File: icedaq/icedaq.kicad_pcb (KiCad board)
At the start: 2 copper layers, 53 parts, among them J1 analog outputs, J2 analog inputs, P1 UART, U1 REG12, U2 iCE40HX1K-VQ100, U3 RPi, U4 oscillator4, U5 ADC082S021, U6 ADC082S021, U7 MCP6004

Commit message: icedaq layout
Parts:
- added CD1: C_Small, Capacitors_SMD:C_0603_HandSoldering, F.Cu at (171.6, 81.3)
- added CD11: C_Small, Capacitors_SMD:C_0603_HandSoldering, F.Cu at (178.7, 97.6)
- added CD12: C_Small, Capacitors_SMD:C_0603_HandSoldering, F.Cu at (159.4, 87.1)
- added CD13: C_Small, Capacitors_SMD:C_0603_HandSoldering, F.Cu at (149.8, 63.2)
- added CD3: C_Small, Capacitors_SMD:C_0603_HandSoldering, F.Cu at (189.9, 65.7)
- added CD4: C_Small, Capacitors_SMD:C_0603_HandSoldering, F.Cu at (197.7, 79.6)
- added CD5: C_Small, Capacitors_SMD:C_0603_HandSoldering, F.Cu at (174.8, 80.9)
- added CD6: C_Small, Capacitors_SMD:C_0603_HandSoldering, F.Cu at (169.0, 68.8)
- added CD7: C_Small, Capacitors_SMD:C_0603_HandSoldering, F.Cu at (192.0, 88.3)
- added RB1: 3.9k, Resistors_SMD:R_0603_HandSoldering, F.Cu at (192.0, 65.6)
- added RB2: 3.9k, Resistors_SMD:R_0603_HandSoldering, F.Cu at (193.9, 66.3)
- added REF**: MountingHole_3mm, Mounting_Holes:MountingHole_3mm, F.Cu at (140.1, 58.7)
- added REF**: MountingHole_3mm, Mounting_Holes:MountingHole_3mm, F.Cu at (198.1, 58.7)
- added REF**: MountingHole_3mm, Mounting_Holes:MountingHole_3mm, F.Cu at (198.1, 107.7)
- added REF**: MountingHole_3mm, Mounting_Holes:MountingHole_3mm, F.Cu at (140.1, 107.7)
- added ROM1: CAT24C, Housings_SOIC:SOIC-8_3.9x4.9mm_Pitch1.27mm, F.Cu at (197.9, 65.6)
- moved R20 50.3 mm to (163.6, 108.5), turned to 0 degrees
- moved R22 46.6 mm to (157.4, 108.7), turned to 0 degrees
- moved D5 42.6 mm to (148.4, 102.2), turned to 270 degrees
- moved D6 42.3 mm to (150.7, 106.0)
- moved J2 42.2 mm to (140.8, 63.9)
- moved J1 40.5 mm to (140.6, 95.6)
- moved D3 39.7 mm to (151.8, 72.2), turned to 0 degrees
- moved D4 38.7 mm to (153.9, 75.2), turned to 0 degrees
- moved R1 38.5 mm to (186.4, 96.3)
- moved U4 37.4 mm to (186.5, 92.1), turned to 180 degrees
- moved R4 36.8 mm to (158.2, 103.1), turned to 180 degrees
- moved R3 36.7 mm to (158.1, 100.7), turned to 0 degrees
- moved R18 36.5 mm to (163.0, 103.1), turned to 0 degrees
- moved R17 36.4 mm to (163.1, 100.7), turned to 180 degrees
- moved R12 36.1 mm to (153.9, 78.0), turned to 180 degrees
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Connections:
- R1 pad 1: +3V3 -> Net-(R1-Pad1)
- R1 pad 2: Net-(R1-Pad2) -> +3V3
- U2 pad 30: /GCLK2 -> (no net)
- U2 pad 37: /MISO1 -> /SCLK1
- U2 pad 41: /SCLK1 -> /MISO1
- U2 pad 63: /Analog/clk -> GCLK2
- U2 pad 65: /Analog/din3 -> (no net)
- U2 pad 66: /Analog/slkc3 -> (no net)
- U2 pad 68: /Analog/sync3 -> (no net)
- U2 pad 71: /Analog/din4 -> (no net)
- U2 pad 72: /Analog/sclk4 -> (no net)
- U2 pad 73: /Analog/sync4 -> (no net)
- U2 pad 78: (no net) -> /Analog/din3
- U2 pad 79: (no net) -> /Analog/slkc3
- U2 pad 80: (no net) -> /Analog/sync3
- U2 pad 82: (no net) -> /Analog/din4
- U2 pad 83: (no net) -> /Analog/sclk4
- U2 pad 85: (no net) -> /Analog/sync4
- U2 pad 90: (no net) -> clk
- U3 pad 27: (no net) -> /ID_SD
- U3 pad 28: (no net) -> /ID_SC
- U3 pad 31: /GCLK2 -> /GCLK0
- U3 pad 7: /GCLK0 -> GCLK2
- U4 pad 1: Net-(R1-Pad2) -> Net-(R1-Pad1)
- U4 pad 3: /Analog/clk -> clk
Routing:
- net +3V3: track 0.00 -> 215.8 mm, vias 0 -> 5
- net GND: track 0.00 -> 107.5 mm, vias 0 -> 33
- net +5V: track 0.00 -> 85.7 mm, vias 0 -> 4
- net +1V2: track 0.00 -> 62.7 mm
- net /SS1: track 0.00 -> 38.3 mm, vias 0 -> 1
- net /CDONE: track 0.00 -> 36.2 mm, vias 0 -> 1
- net /Analog/in4a: track 0.00 -> 33.8 mm, vias 0 -> 3
- net /Analog/in2a: track 0.00 -> 33.7 mm, vias 0 -> 1
- net GCLK2: track 0.00 -> 33.6 mm, vias 0 -> 1
- net /CRST: track 0.00 -> 31.4 mm, vias 0 -> 1
- net /ID_SC: track 0.00 -> 31.3 mm
- net /ID_SD: track 0.00 -> 28.5 mm, vias 0 -> 2
- net /Analog/out4: track 0.00 -> 25.3 mm
- net /Analog/in1: track 0.00 -> 24.9 mm, vias 0 -> 1
- net /MOSI: track 0.00 -> 20.8 mm, vias 0 -> 1
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- added copper zone on B.Cu, net GND
- added copper zone on F.Cu, net GND
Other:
- board outline added: 65.3 x 56.4 mm
- net class Default: clearance 0.2 -> 0.1524; trace_width 0.25 -> 0.1778; via_dia 0.6 -> 0.5588; via_drill 0.4 -> 0.381
- net class Ground added: clearance 0.1524, trace_width 0.1778, via_dia 0.5588, via_drill 0.381
- net class Power added: clearance 0.2032, trace_width 0.3556, via_dia 0.762, via_drill 0.4826
- rule trace_clearance: 0.2 -> 0.1524
- rule trace_min: 0.2 -> 0.1524
- rule via_min_drill: 0.3 -> 0.3302
- rule via_min_size: 0.4 -> 0.508

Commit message: icedaq more
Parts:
- added P2: GPIO, Pin_Headers:Pin_Header_Straight_1x05_Pitch2.00mm, F.Cu at (199.0, 80.0)
- moved CD4 4.53 mm to (197.5, 84.1)
- moved U6 0.15 mm to (170.4, 72.1)
- moved U5 0.07 mm to (170.3, 77.0)
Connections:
- U2 pad 20: (no net) -> Net-(P2-Pad1)
- U2 pad 21: (no net) -> Net-(P2-Pad2)
- U2 pad 24: (no net) -> Net-(P2-Pad3)
- U2 pad 25: (no net) -> Net-(P2-Pad4)
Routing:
- net GND: track 107.5 -> 130.4 mm, vias 33 -> 41
- net Net-(P2-Pad1): track 0.00 -> 8.84 mm
- net Net-(P2-Pad3): track 0.00 -> 7.55 mm
- net Net-(P2-Pad2): track 0.00 -> 7.34 mm
- net Net-(P2-Pad4): track 0.00 -> 5.94 mm
- net +1V2: track 62.7 -> 60.6 mm
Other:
- outline, holes or cut-outs redrawn

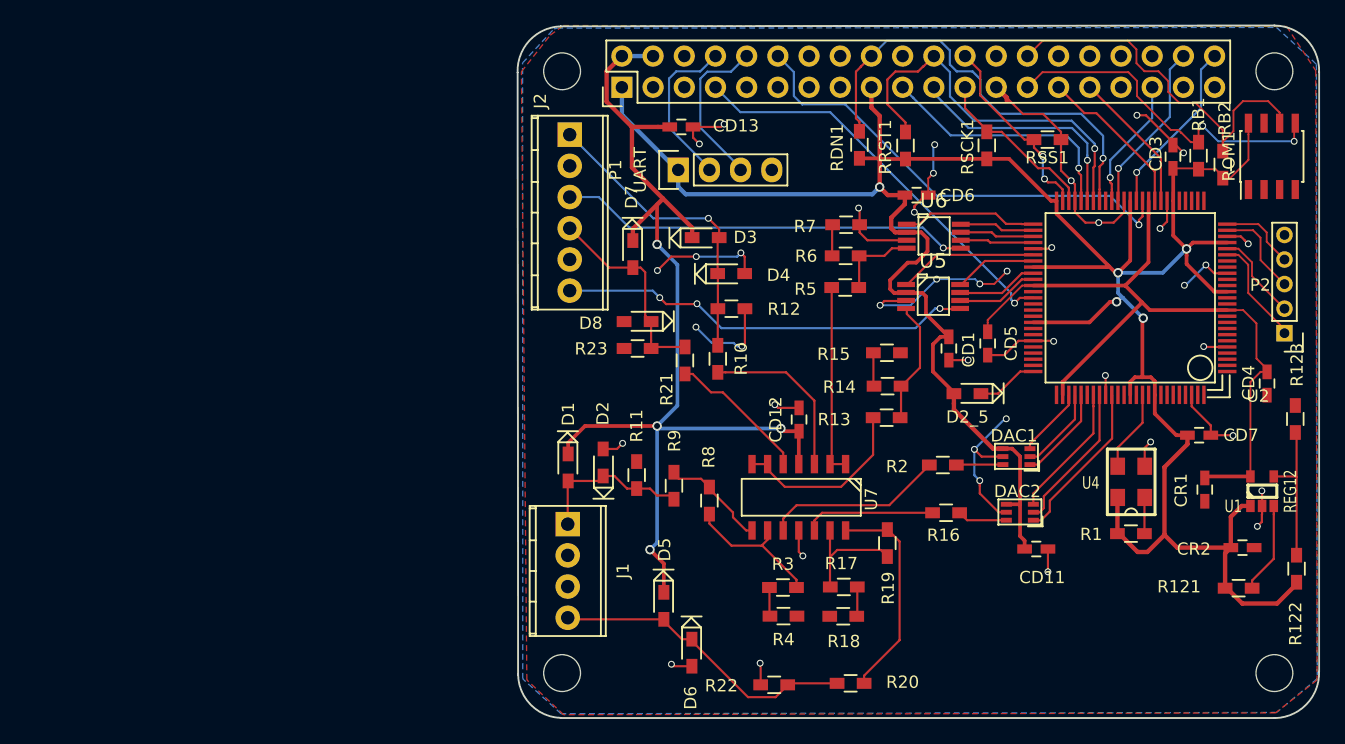
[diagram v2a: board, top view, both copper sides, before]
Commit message: icedaq: change input filter
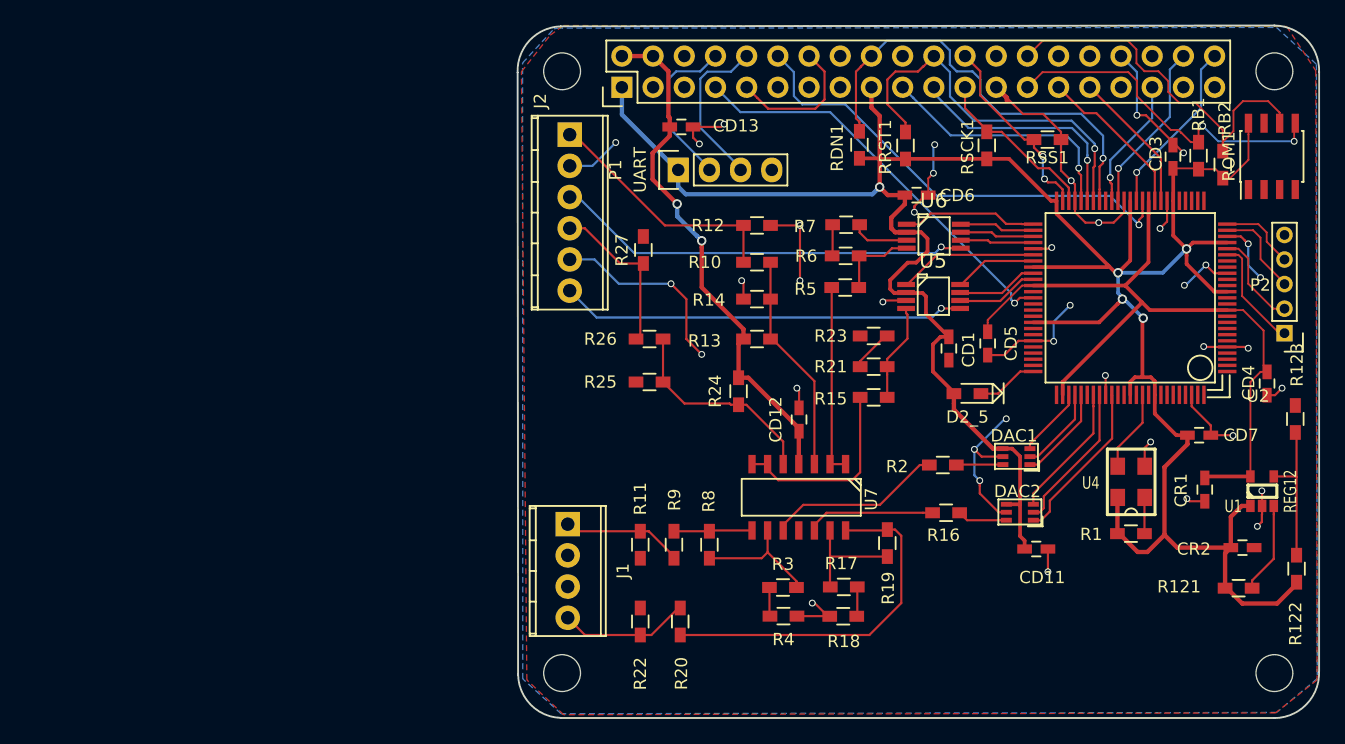
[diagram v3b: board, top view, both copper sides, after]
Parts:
- removed D1, D2, D3, D4, D5, D6, D7, D8: D_Small, local:D_0603_HandSoldering
- added R24: R, Resistors_SMD:R_0603_HandSoldering, F.Cu at (154.5, 84.8)
- added R25: R, Resistors_SMD:R_0603_HandSoldering, F.Cu at (147.2, 84.0)
- added R26: R, Resistors_SMD:R_0603_HandSoldering, F.Cu at (147.2, 80.5)
- added R27: R, Resistors_SMD:R_0603_HandSoldering, F.Cu at (146.8, 73.2)
- R13, R14: value 1k -> R
- R21, R23: value R -> 1k
- moved R23 19.2 mm to (165.5, 80.2)
- moved R21 15.4 mm to (165.5, 82.8), turned to 0 degrees
- moved R20 14.8 mm to (149.8, 103.5), turned to 270 degrees
- moved R14 12.8 mm to (156.0, 77.2)
- moved R13 12.3 mm to (156.0, 80.5)
- moved R22 12.1 mm to (146.5, 103.5), turned to 270 degrees
- moved R10 8.49 mm to (156.0, 74.2), turned to 0 degrees
- moved R12 7.09 mm to (156.0, 71.2)
- moved R11 5.68 mm to (146.5, 97.2), turned to 90 degrees
- moved R9 4.80 mm to (149.2, 97.2)
- moved R15 3.79 mm to (165.5, 85.2)
- moved R8 3.60 mm to (152.1, 97.2)
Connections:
- R13 pad 1: /Analog/in3a -> Net-(R10-Pad2)
- R13 pad 2: Net-(R13-Pad2) -> +5V
- R14 pad 1: Net-(R14-Pad1) -> GND
- R14 pad 2: /Analog/in3a -> Net-(R10-Pad2)
- R15 pad 1: GND -> /Analog/in3a
- R15 pad 2: Net-(R14-Pad1) -> Net-(R15-Pad2)
- R21 pad 1: /Analog/in3 -> Net-(R21-Pad1)
- R21 pad 2: Net-(R21-Pad2) -> /Analog/in3a
- R23 pad 2: /Analog/in3 -> Net-(R21-Pad1)
- U7 pad 5: Net-(R21-Pad2) -> Net-(R24-Pad1)
- U7 pad 6: Net-(R13-Pad2) -> Net-(R15-Pad2)
- U7 pad 7: Net-(R13-Pad2) -> Net-(R15-Pad2)
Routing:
- net +5V: track 85.7 -> 42.6 mm, vias 4 -> 2
- net GND: track 130.4 -> 152.1 mm, vias 41 -> 39
- net Net-(R24-Pad1): track 0.00 -> 17.1 mm
- net Net-(R15-Pad2): track 0.00 -> 16.0 mm
- net Net-(R13-Pad2): track 15.0 -> 0.00 mm
- net /Analog/out4: track 25.3 -> 10.7 mm
- net Net-(R19-Pad2): track 17.6 -> 29.3 mm
- net Net-(R21-Pad2): track 11.6 -> 0.00 mm
- net /Analog/in1: track 24.9 -> 20.2 mm, vias 1 -> 0
- net Net-(R10-Pad2): track 14.0 -> 18.0 mm
- net Net-(R21-Pad1): track 0.00 -> 3.50 mm
- net /Analog/in3: track 16.8 -> 13.6 mm
- net /Analog/out3: track 13.1 -> 9.89 mm
- net Net-(R14-Pad1): track 2.74 -> 0.00 mm
- net Net-(R8-Pad2): track 8.72 -> 6.38 mm
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
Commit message: icedaq: update
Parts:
- added TP1: WP, local:testpoint, F.Cu at (175.4, 62.4)
- J2: footprint Terminal_Blocks:TerminalBlock_Pheonix_MPT-2.54mm_6pol -> Terminal_Blocks:TerminalBlock_Pheonix_MPT-2.54mm_4pol
- moved CD7 23.3 mm to (199.2, 66.2), turned to 90 degrees
- moved RB2 23.2 mm to (170.8, 67.4)
- moved ROM1 22.0 mm to (176.0, 67.0)
- moved RSCK1 21.7 mm to (196.4, 65.6)
- moved CD5 17.7 mm to (187.6, 68.6), turned to 90 degrees
- moved RB1 11.4 mm to (180.6, 66.4)
- moved CD3 10.8 mm to (198.8, 71.8), turned to 0 degrees
- moved CD4 9.19 mm to (192.8, 92.0), turned to 180 degrees
- moved CR2 6.72 mm to (192.0, 103.2)
- moved R123 6.70 mm to (199.4, 93.7)
- moved R121 6.30 mm to (192.0, 106.2)
- moved U1 6.17 mm to (193.9, 99.8)
- moved P2 5.78 mm to (199.2, 85.8)
- moved CD11 5.29 mm to (177.8, 102.8)
- moved RSS1 4.80 mm to (184.2, 65.8), turned to 90 degrees
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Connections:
- J2 pad 3: /Analog/in2a -> GND
- ROM1 pad 7: (no net) -> Net-(ROM1-Pad7)
- U2 pad 1: (no net) -> Net-(U2-Pad1)
- U2 pad 10: (no net) -> Net-(P2-Pad4)
- U2 pad 100: (no net) -> Net-(U2-Pad100)
- U2 pad 12: (no net) -> Net-(U2-Pad12)
- U2 pad 13: (no net) -> Net-(U2-Pad13)
- U2 pad 15: (no net) -> Net-(U2-Pad15)
- U2 pad 16: (no net) -> Net-(U2-Pad16)
- U2 pad 18: (no net) -> Net-(U2-Pad18)
- U2 pad 19: (no net) -> Net-(U2-Pad19)
- U2 pad 2: (no net) -> Net-(U2-Pad2)
- U2 pad 20: Net-(P2-Pad1) -> Net-(U2-Pad20)
- U2 pad 21: Net-(P2-Pad2) -> Net-(U2-Pad21)
- U2 pad 24: Net-(P2-Pad3) -> Net-(U2-Pad24)
- U2 pad 25: Net-(P2-Pad4) -> Net-(U2-Pad25)
- U2 pad 26: (no net) -> Net-(U2-Pad26)
- U2 pad 27: (no net) -> Net-(U2-Pad27)
- U2 pad 28: (no net) -> Net-(U2-Pad28)
- U2 pad 29: (no net) -> Net-(U2-Pad29)
- U2 pad 3: (no net) -> Net-(U2-Pad3)
- U2 pad 30: (no net) -> Net-(U2-Pad30)
- U2 pad 36: /SS1 -> Net-(U2-Pad36)
- U2 pad 37: /SCLK1 -> Net-(U2-Pad37)
- U2 pad 4: (no net) -> Net-(U2-Pad4)
- U2 pad 40: /MOSI1 -> Net-(U2-Pad40)
- U2 pad 41: /MISO1 -> Net-(U2-Pad41)
- U2 pad 42: (no net) -> Net-(U2-Pad42)
- U2 pad 51: /Analog/cs1 -> SS1
- U2 pad 52: /Analog/sclk1 -> SCLK1
- U2 pad 53: /Analog/dout1 -> MISO1
- U2 pad 54: /Analog/din1 -> MOSI1
- U2 pad 56: /Analog/cs2 -> /Analog/cs5
- U2 pad 57: /Analog/sclk2 -> /Analog/sclk5
- U2 pad 59: /Analog/dout2 -> /Analog/dout5
- U2 pad 60: /Analog/din2 -> /Analog/din5
- U2 pad 62: (no net) -> Net-(U2-Pad62)
- U2 pad 63: GCLK2 -> Net-(U2-Pad63)
- U2 pad 64: (no net) -> /Analog/cs6
- U2 pad 65: (no net) -> /Analog/sclk6
- U2 pad 66: (no net) -> /Analog/dout6
- U2 pad 68: (no net) -> /Analog/din6
- U2 pad 69: (no net) -> Net-(U2-Pad69)
- U2 pad 7: (no net) -> Net-(P2-Pad1)
- U2 pad 71: (no net) -> Net-(U2-Pad71)
- U2 pad 72: (no net) -> Net-(U2-Pad72)
- U2 pad 73: (no net) -> Net-(U2-Pad73)
- U2 pad 74: (no net) -> Net-(U2-Pad74)
- U2 pad 76: (no net) -> Net-(U2-Pad76)
- U2 pad 8: (no net) -> Net-(P2-Pad2)
- U2 pad 81: (no net) -> Net-(U2-Pad81)
- U2 pad 86: (no net) -> Net-(U2-Pad86)
- U2 pad 87: (no net) -> Net-(U2-Pad87)
- U2 pad 89: (no net) -> Net-(U2-Pad89)
- U2 pad 9: (no net) -> Net-(P2-Pad3)
- U2 pad 93: (no net) -> Net-(U2-Pad93)
- U2 pad 94: (no net) -> Net-(U2-Pad94)
- U2 pad 95: (no net) -> Net-(U2-Pad95)
- U2 pad 96: (no net) -> Net-(U2-Pad96)
- U2 pad 97: (no net) -> Net-(U2-Pad97)
- U2 pad 99: (no net) -> Net-(U2-Pad99)
- U3 pad 11: (no net) -> Net-(U3-Pad11)
- U3 pad 12: /SS1 -> Net-(U3-Pad12)
- U3 pad 13: (no net) -> Net-(U3-Pad13)
- U3 pad 15: (no net) -> Net-(U3-Pad15)
- U3 pad 16: (no net) -> Net-(U3-Pad16)
- U3 pad 19: /MOSI -> MOSI1
- U3 pad 21: /MISO -> MISO1
- U3 pad 23: /SCK -> SCLK1
- U3 pad 24: /SS -> SS1
- U3 pad 26: (no net) -> Net-(U3-Pad26)
- U3 pad 3: (no net) -> Net-(U3-Pad3)
- U3 pad 32: (no net) -> Net-(U3-Pad32)
- U3 pad 33: (no net) -> Net-(U3-Pad33)
- U3 pad 35: /MISO1 -> /MISO
- U3 pad 36: (no net) -> /SS
- U3 pad 37: (no net) -> Net-(U3-Pad37)
- U3 pad 38: /MOSI1 -> /MOSI
- U3 pad 40: /SCLK1 -> /SCK
- U3 pad 5: (no net) -> Net-(U3-Pad5)
- U3 pad 7: GCLK2 -> Net-(U3-Pad7)
- U5 pad 1: /Analog/cs2 -> /Analog/cs6
- U5 pad 5: /Analog/in4a -> Net-(U5-Pad5)
- U5 pad 6: /Analog/din2 -> /Analog/din6
- U5 pad 7: /Analog/dout2 -> /Analog/dout6
- U5 pad 8: /Analog/sclk2 -> /Analog/sclk6
- U6 pad 1: /Analog/cs1 -> /Analog/cs5
- U6 pad 5: /Analog/in2a -> Net-(U6-Pad5)
- U6 pad 6: /Analog/din1 -> /Analog/din5
- U6 pad 7: /Analog/dout1 -> /Analog/dout5
- U6 pad 8: /Analog/sclk1 -> /Analog/sclk5
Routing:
- net +3V3: track 215.9 -> 0.00 mm, vias 5 -> 0
- net GND: track 152.1 -> 0.00 mm, vias 39 -> 0
- net +1V2: track 60.6 -> 0.00 mm
- net +5V: track 42.6 -> 0.00 mm, vias 2 -> 0
- net /SS1: track 38.3 -> 0.00 mm, vias 1 -> 0
- net /CDONE: track 36.2 -> 0.00 mm, vias 1 -> 0
- net /Analog/in2a: track 34.0 -> 0.00 mm, vias 1 -> 0
- net GCLK2: track 33.6 -> 0.00 mm, vias 1 -> 0
- net /Analog/in4a: track 33.0 -> 0.00 mm, vias 1 -> 0
- net /CRST: track 31.4 -> 0.00 mm, vias 1 -> 0
- net /ID_SC: track 31.3 -> 0.00 mm
- net Net-(R19-Pad2): track 29.3 -> 0.00 mm
- net /ID_SD: track 28.5 -> 0.00 mm, vias 2 -> 0
- net /MOSI: track 20.8 -> 0.00 mm, vias 1 -> 0
- net /Analog/in1: track 20.2 -> 0.00 mm
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
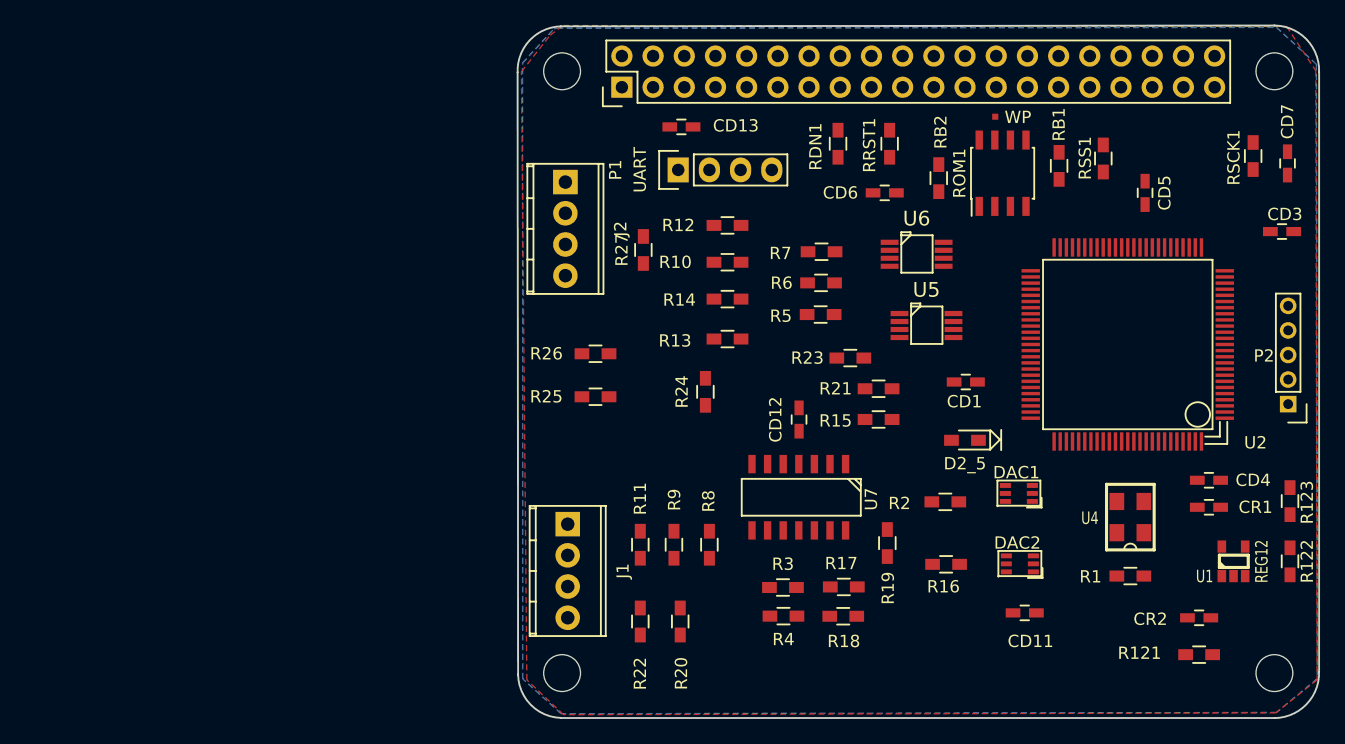
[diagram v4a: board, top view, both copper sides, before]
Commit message: icedaq: layout take 2
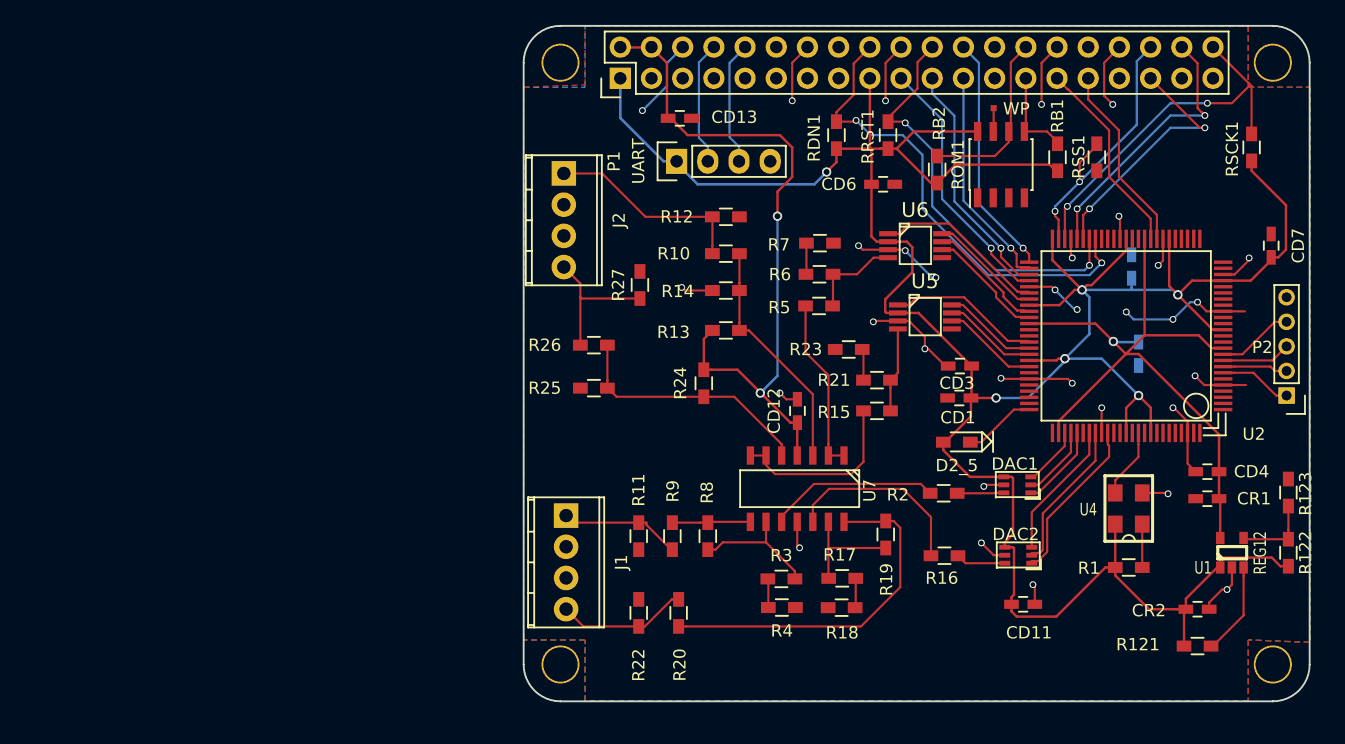
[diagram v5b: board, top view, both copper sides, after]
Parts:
- added CD2: C_Small, Capacitors_SMD:C_0603_HandSoldering, B.Cu at (186.5, 74.6)
- CD5: moved to B.Cu
- moved CD3 28.4 mm to (172.5, 82.7), turned to 180 degrees
- moved CD5 13.1 mm to (187.1, 81.7), turned to 270 degrees
- moved CD7 6.83 mm to (197.9, 72.9)
- moved R27 2.86 mm to (146.5, 76.1)
- moved CD1 1.40 mm to (172.5, 85.3)
- moved U3 0.74 mm to (144.9, 59.3)
- moved CD11 0.71 mm to (177.7, 102.1)
- moved CD4 0.71 mm to (192.7, 91.3)
- moved CR1 0.71 mm to (192.7, 93.5)
- moved DAC1 0.71 mm to (177.2, 92.4)
- moved R19 0.71 mm to (166.5, 96.4)
- moved R2 0.71 mm to (171.2, 93.1)
- moved R24 0.71 mm to (151.7, 84.1)
- moved RB2 0.71 mm to (170.7, 66.7)
- moved U5 0.71 mm to (169.7, 78.7)
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- renumbered REF** to MNT1
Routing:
- net +3V3: track 0.00 -> 233.1 mm, vias 0 -> 6
- net GND: track 0.00 -> 103.6 mm, vias 0 -> 32
- net +5V: track 0.00 -> 56.7 mm, vias 0 -> 2
- net +1V2: track 0.00 -> 55.3 mm, vias 0 -> 1
- net /CDONE: track 0.00 -> 39.2 mm, vias 0 -> 2
- net /CRST: track 0.00 -> 34.0 mm, vias 0 -> 2
- net /SCK: track 0.00 -> 30.1 mm, vias 0 -> 2
- net Net-(R19-Pad2): track 0.00 -> 29.0 mm
- net /SS: track 0.00 -> 22.6 mm, vias 0 -> 2
- net /MOSI: track 0.00 -> 22.3 mm, vias 0 -> 2
- net MOSI1: track 0.00 -> 21.3 mm, vias 0 -> 1
- net /MISO: track 0.00 -> 20.9 mm, vias 0 -> 2
- net Net-(R24-Pad1): track 0.00 -> 20.5 mm
- net MISO1: track 0.00 -> 19.7 mm, vias 0 -> 1
- net SS1: track 0.00 -> 19.7 mm, vias 0 -> 1
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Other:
- board size 65.3 x 56.4 mm -> 64 x 55 mm
- net class Default: clearance 0.1524 -> 0.1778
- net class Ground: clearance 0.1524 -> 0.1778
- net class Power: trace_width 0.3556 -> 0.2
- rule trace_clearance: 0.1524 -> 0.1778
- rule via_min_drill: 0.3302 -> 0.127
- rule via_min_size: 0.508 -> 0.381
